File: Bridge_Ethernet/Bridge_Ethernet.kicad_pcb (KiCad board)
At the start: 2 copper layers, 62 x 82 mm, 82 parts, among them J1 Conn_01x04_Female, J2 Conn_01x04_Female, J3 Conn_01x06, J4 Conn_01x06, J5 Conn_2Rows-13Pins, J7 Conn_01x04_Male, U1 MAX3222CDW, U10 MAX3222CDW, U11 ISL83485, U12 MAX3222CDW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

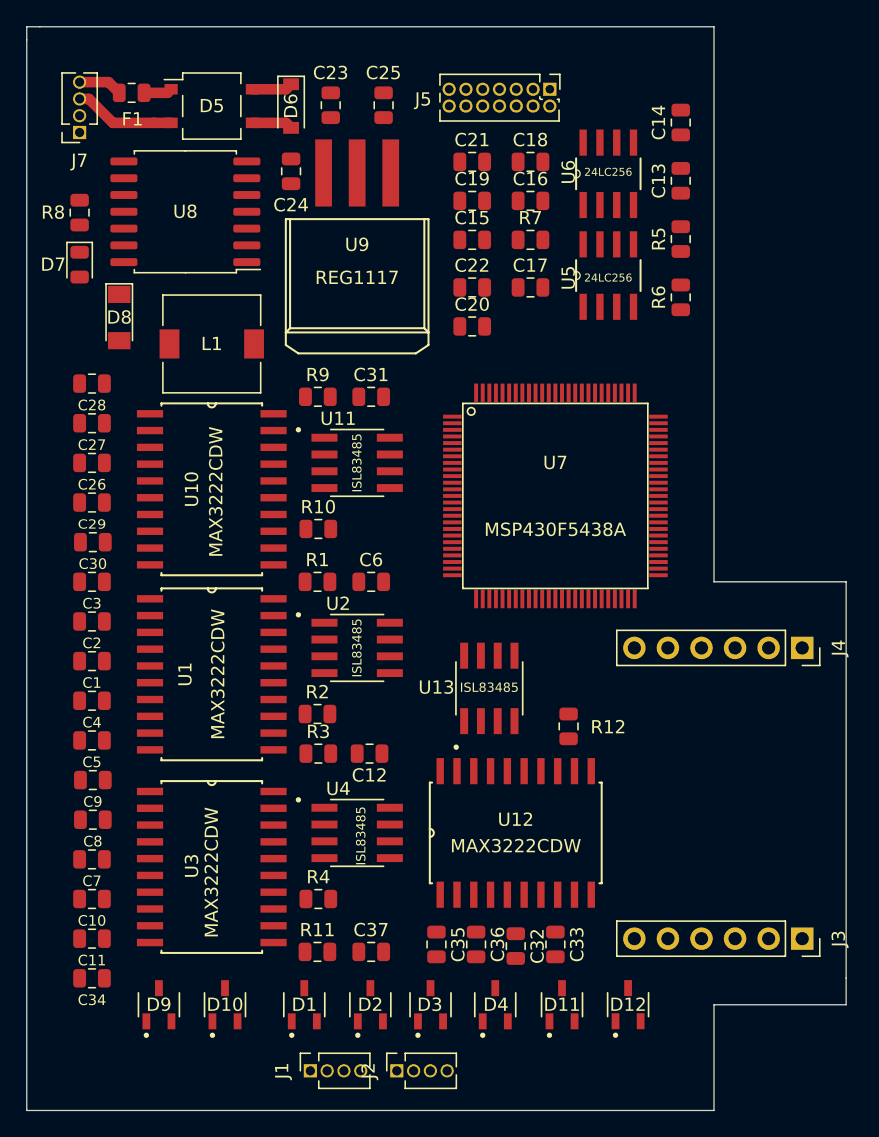
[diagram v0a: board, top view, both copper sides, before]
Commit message: Esquemático Finalizado. Asignaciones Realizadas. Reacomodamiento de componentes. Ruteo en Proceso.
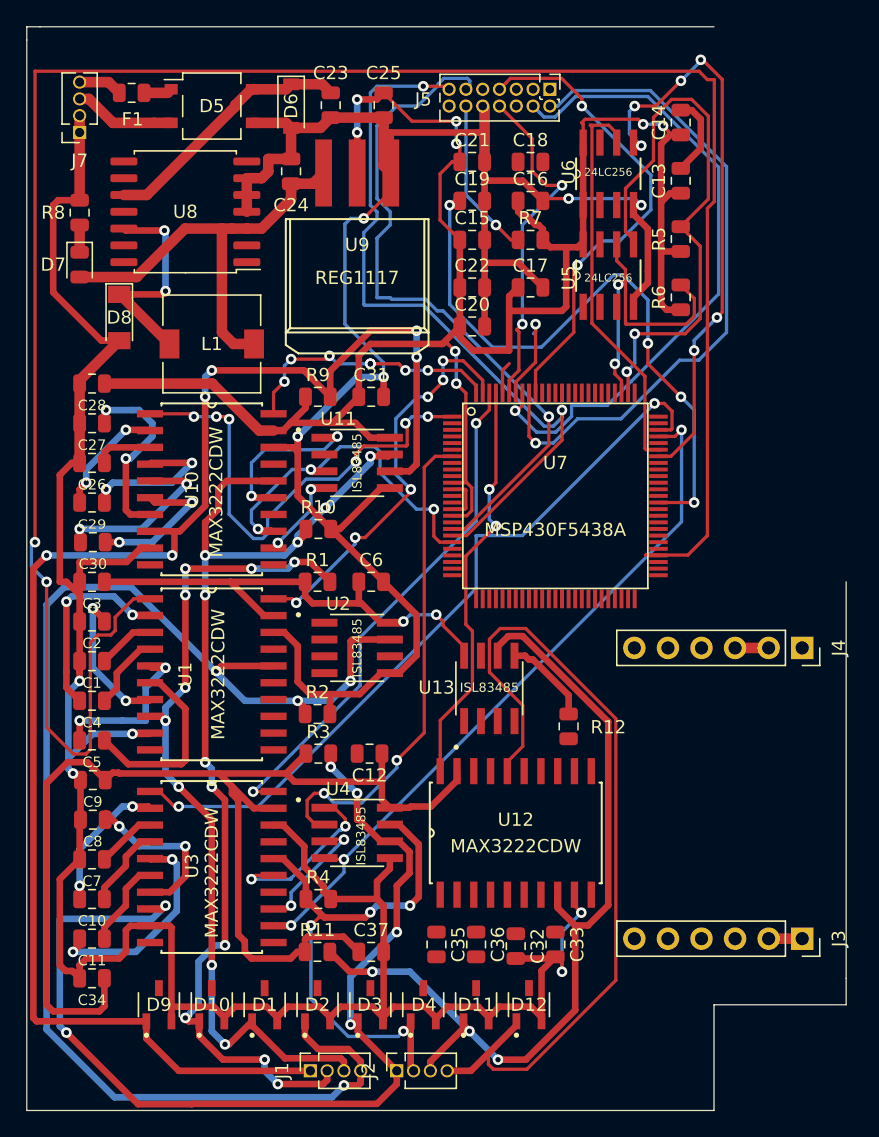
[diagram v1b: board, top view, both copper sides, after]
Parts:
- moved D12 7.50 mm to (59.0, 147.0)
- moved D11 6.50 mm to (55.0, 147.0)
- moved D4 5.45 mm to (51.0, 147.0)
- moved D3 4.55 mm to (47.0, 147.0)
- moved D2 4.00 mm to (43.0, 147.0)
- moved D1 3.00 mm to (39.0, 147.0)
- moved D10 1.00 mm to (35.0, 147.0)
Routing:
- net GND: track 3.08 -> 354.8 mm, vias 0 -> 10
- net +3V3: track 0.00 -> 282.7 mm, vias 0 -> 10
- net /RX1: track 0.00 -> 161.7 mm, vias 0 -> 2
- net /A_485_0: track 0.00 -> 117.5 mm, vias 0 -> 6
- net /B_485_1: track 0.00 -> 105.7 mm, vias 0 -> 4
- net /B_485_0: track 0.00 -> 80.9 mm, vias 0 -> 11
- net /A_485_2: track 0.00 -> 78.8 mm, vias 0 -> 6
- net /B_485_3: track 0.00 -> 67.4 mm
- net /A_485_3: track 0.00 -> 67.4 mm, vias 0 -> 3
- net /A_485_1: track 0.00 -> 63.4 mm, vias 0 -> 9
- net /RX2: track 0.00 -> 57.6 mm, vias 0 -> 2
- net /Microcontrolador/BSL_RX: track 0.00 -> 56.1 mm, vias 0 -> 2
- net /TX2: track 0.00 -> 54.5 mm, vias 0 -> 3
- net /Microcontrolador/BSL_TX: track 0.00 -> 52.5 mm, vias 0 -> 1
- net /Microcontrolador/MICRO_TD0_1: track 0.00 -> 50.7 mm, vias 0 -> 1
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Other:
- outline, holes or cut-outs redrawn
- net class Default2 added: clearance 0.2, trace_width 0.8, via_dia 0.8, via_drill 0.4

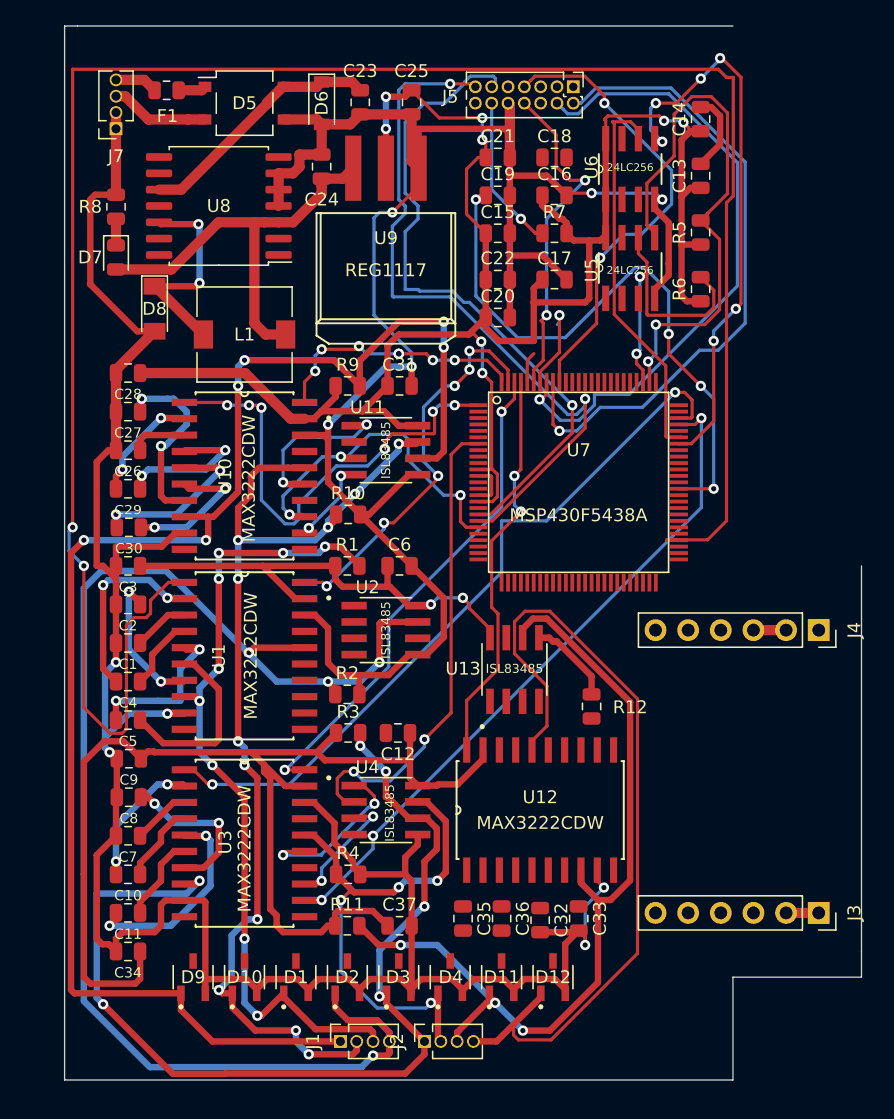
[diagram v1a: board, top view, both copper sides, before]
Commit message: Esquemático Finalizado. Asignaciones Realizadas. Reacomodamiento de componentes. Ruteo Finalizado.
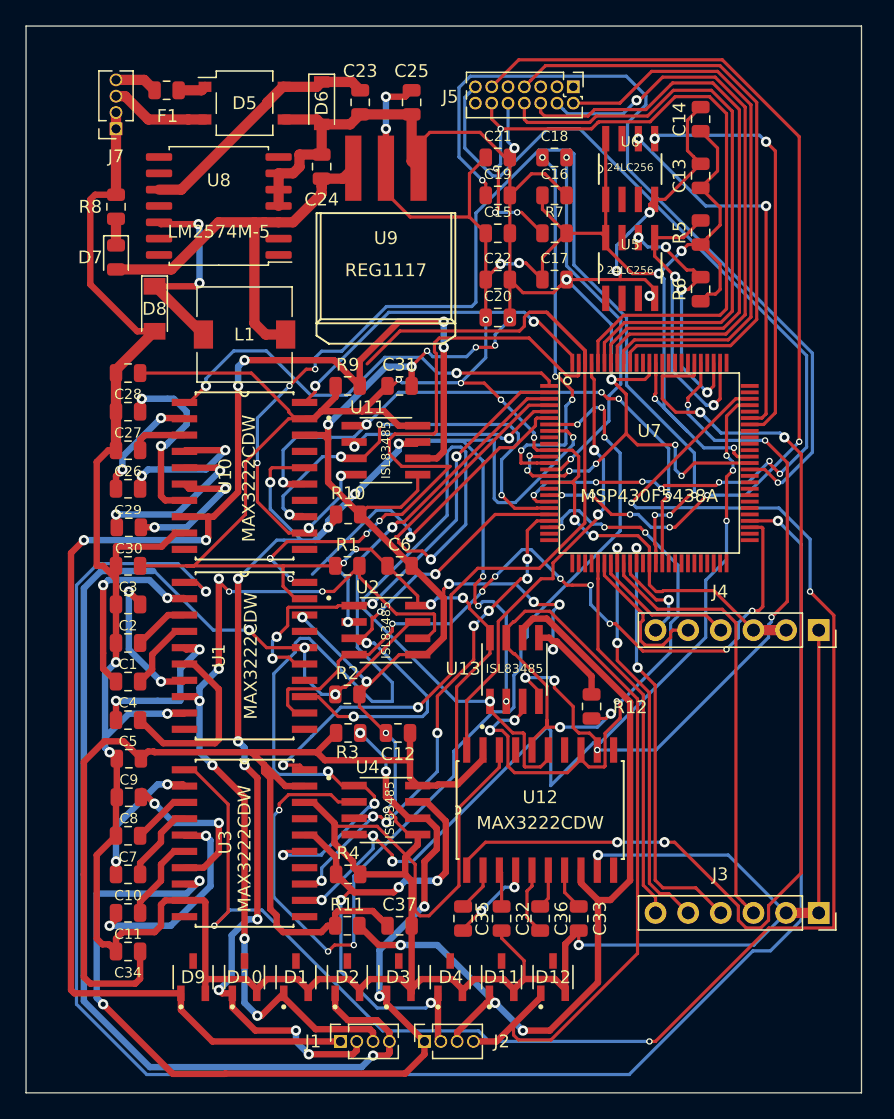
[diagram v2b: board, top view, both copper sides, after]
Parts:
- moved U7 5.70 mm to (66.5, 107.0)
- moved C32 3.00 mm to (55.0, 142.4)
- moved C36 3.00 mm to (58.0, 142.4)
- turned C35 to 90 degrees
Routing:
- net GND: track 354.8 -> 499.7 mm, vias 10 -> 31
- net /TX0: track 6.68 -> 93.8 mm, vias 2 -> 8
- net /RX3: track 0.00 -> 84.0 mm, vias 0 -> 4
- net /RX2: track 57.6 -> 129.8 mm, vias 2 -> 4
- net /232_3: track 0.00 -> 68.2 mm, vias 0 -> 2
- net +3V3: track 282.7 -> 346.5 mm, vias 10 -> 19
- net /232_2: track 13.1 -> 72.5 mm, vias 2 -> 4
- net /TX1: track 0.00 -> 58.5 mm, vias 0 -> 8
- net /TX3: track 0.00 -> 56.7 mm, vias 0 -> 6
- net /RTS3: track 0.00 -> 48.2 mm, vias 0 -> 6
- net /485_3: track 0.00 -> 46.5 mm, vias 0 -> 4
- net /Microcontrolador/MICRO_RTS_1: track 14.5 -> 60.5 mm, vias 1 -> 4
- net /485_2: track 37.2 -> 78.3 mm, vias 2 -> 6
- net /Microcontrolador/MICRO_TMS_1: track 6.61 -> 46.4 mm, vias 1 -> 0
- net /RTS1: track 0.00 -> 38.8 mm, vias 0 -> 4
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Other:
- board size 62 x 82 mm -> 65 x 83 mm
- board text added: "ALIMENTACIÓN"
- board text added: "DRIVERS SERIE"
- board text added: "ETHERNET"
- board text added: "LM2574M-5"
- board text added: "MEMORIAS"
- board text added: "PROTECCIONES"

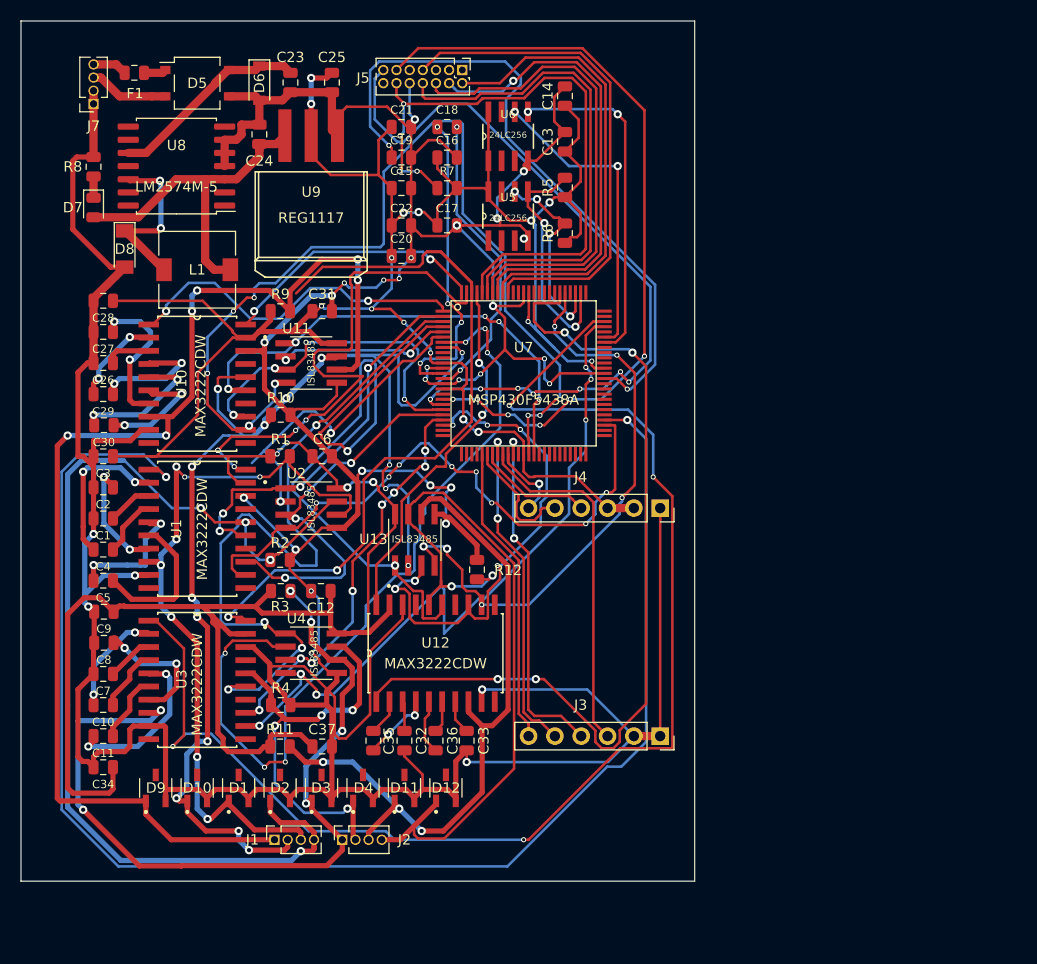
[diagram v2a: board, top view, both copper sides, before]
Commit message: v2.0. Faltan algunos componentes 3D. Correciones relizadas.
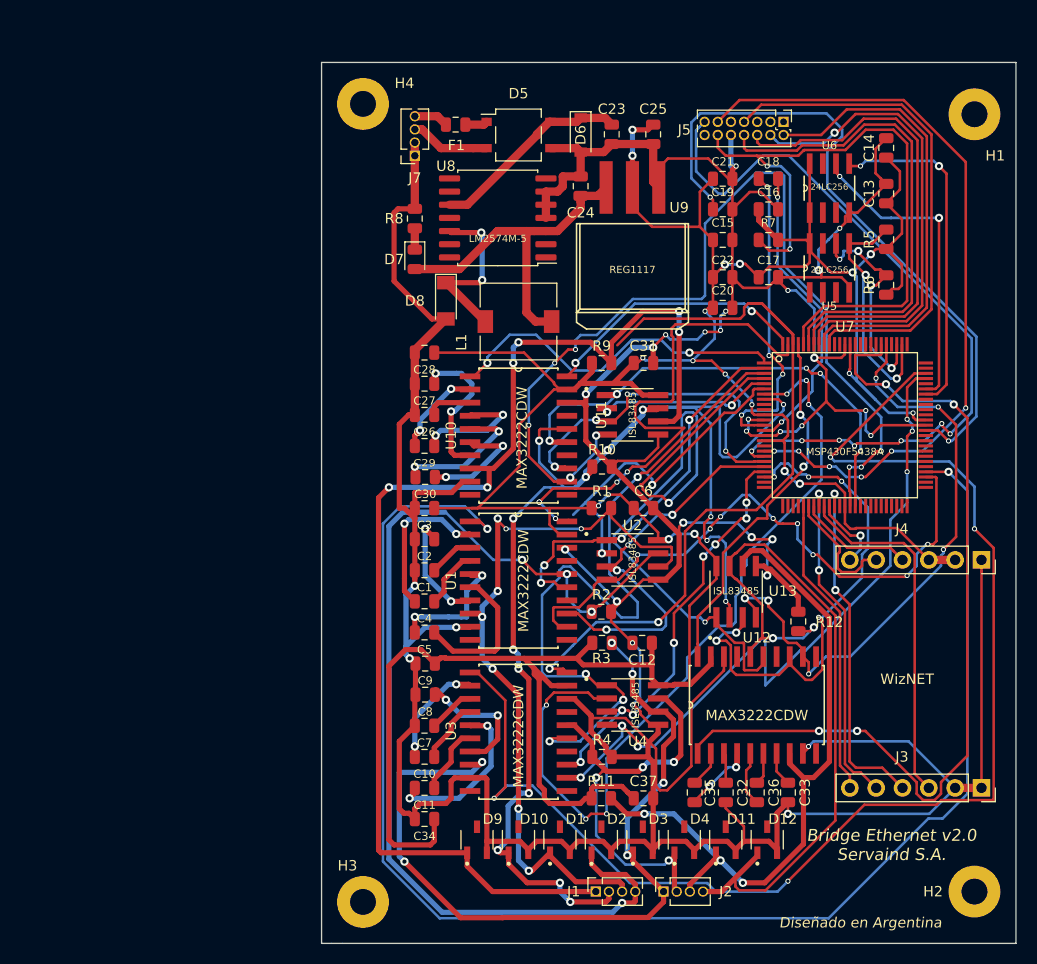
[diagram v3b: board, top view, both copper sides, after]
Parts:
- added H1: MountingHole, MountingHole:MountingHole_2.5mm_Pad, F.Cu at (110.0, 82.0)
- added H2: MountingHole, MountingHole:MountingHole_2.5mm_Pad, F.Cu at (110.0, 157.0)
- added H3: MountingHole, MountingHole:MountingHole_2.5mm_Pad, F.Cu at (51.0, 158.0)
- added H4: MountingHole, MountingHole:MountingHole_2.5mm_Pad, F.Cu at (51.0, 81.0)
- moved C16 31.4 mm to (90.1, 91.2)
- moved C17 31.4 mm to (90.1, 97.7)
- moved C18 31.4 mm to (90.1, 88.2)
- moved R7 31.4 mm to (90.1, 94.1)
- moved C1 31.4 mm to (56.9, 126.0)
- moved C10 31.4 mm to (56.9, 144.0)
- moved C11 31.4 mm to (56.9, 147.0)
- moved C12 31.4 mm to (77.9, 133.0)
- moved C13 31.4 mm to (101.5, 89.7)
- moved C14 31.4 mm to (101.5, 85.2)
- moved C2 31.4 mm to (56.9, 123.0)
- moved C23 31.4 mm to (75.0, 83.9)
- moved C24 31.4 mm to (72.0, 88.9)
- moved C25 31.4 mm to (79.0, 83.9)
- moved C26 31.4 mm to (56.9, 111.0)
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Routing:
- net +3V3: track 346.5 -> 350.7 mm
- net /Microcontrolador/MICRO_RTS_1: track 60.5 -> 63.9 mm, vias 4 -> 2
- net /TX3: track 56.7 -> 58.8 mm
- net /RTS3: track 48.2 -> 50.1 mm
- net /Memorias/SCL1: track 19.4 -> 21.1 mm
- net /Memorias/SCL2: track 29.7 -> 30.3 mm
- net GND: track 499.7 -> 500.1 mm, vias 31 -> 30
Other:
- board size 65 x 83 mm -> 67 x 85 mm
- board text added: "Bridge Ethernet v2.0 Servaind S.A."
- board text added: "Diseñado en Argentina"
- board text added: "Grillas: 1 mm/0,5 mm/0,25mm Ancho de Pistas: 0,8 mm/0,5 mm/0,25 mm Ancho de vía/agujero de vía: 0,8/0,4 mm y 0,5/0,3 mm Fabricante de Referencia: Mayer Dimensiones en Capa Dwgs.User"
- board text added: "WizNET"

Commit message: Correciones relizadas.
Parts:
- added FID1: Fiducial, Fiducial:Fiducial_0.5mm_Mask1mm, F.Cu at (121.5, 64.0)
- added FID2: Fiducial, Fiducial:Fiducial_0.5mm_Mask1mm, F.Cu at (177.0, 56.0)
- added FID3: Fiducial, Fiducial:Fiducial_0.5mm_Mask1mm, F.Cu at (127.0, 135.0)
- moved C13 74.8 mm to (172.5, 66.2)
- moved C14 74.8 mm to (172.5, 61.7)
- moved C15 74.8 mm to (156.7, 70.6)
- moved C19 74.8 mm to (156.7, 67.7)
- moved C20 74.8 mm to (156.7, 77.2)
- moved C21 74.8 mm to (156.7, 64.7)
- moved C22 74.8 mm to (156.7, 74.2)
- moved J1 74.8 mm to (144.5, 133.5)
- moved J3 74.8 mm to (181.7, 123.5)
- moved J4 74.8 mm to (181.7, 101.5)
- moved J5 74.8 mm to (162.6, 59.2)
- moved R5 74.8 mm to (172.5, 70.6)
- moved R6 74.8 mm to (172.5, 75.0)
- moved U5 74.8 mm to (167.0, 73.3)
- moved U6 74.8 mm to (167.0, 65.6)
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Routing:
- added copper zone on B.Cu, net GND
- added copper zone on F.Cu, net GND
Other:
- board text added: "2019"
